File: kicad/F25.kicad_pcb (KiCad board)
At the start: 2 copper layers, 45 x 30 mm, 37 parts, among them J3 B2B-PH-K-S, J4 USB_C_Receptacle_USB2.0_16P, Q1 IRLML6244, SW1 RESET, SW2 BOOT, U1 MS5611-01BA, U2 MPU-6050, U4 ESP32-S3-WROOM-1-N8, U5 AP2112K-3.3

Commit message: MAJOR UPDATES
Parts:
- removed C11: 1uF, Capacitor_SMD:C_0402_1005Metric
- added C8: 10uF, Capacitor_SMD:C_0402_1005Metric, F.Cu at (177.4, 96.3)
- added Q2: DMG3415U, Package_TO_SOT_SMD:SOT-23, F.Cu at (173.1, 92.9)
- added R8: 100k, Capacitor_SMD:C_0402_1005Metric, F.Cu at (168.2, 107.4)
- added R9: 100k, Capacitor_SMD:C_0402_1005Metric, F.Cu at (163.5, 90.6)
- C10: value 1uF -> 10uF
- R5: value 10k -> 100k
- moved R5 21.5 mm to (177.4, 94.4), turned to 90 degrees
- moved C10 11.1 mm to (171.1, 98.7)
- moved R4 10.1 mm to (169.7, 103.5), turned to 90 degrees
- moved U5 2.05 mm to (173.2, 96.4), turned to 180 degrees
- moved LS1 0.60 mm to (175.7, 103.0), turned to -90 degrees
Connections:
- C1 pad 1: BAT- -> GND
- C10 pad 1: BAT+ -> GND
- C10 pad 2: BAT- -> +3V3
- C2 pad 1: BAT- -> GND
- C3 pad 2: BAT- -> GND
- C4 pad 1: BAT- -> GND
- C5 pad 1: BAT- -> GND
- C6 pad 2: BAT- -> GND
- C7 pad 2: BAT- -> GND
- C9 pad 2: BAT- -> GND
- CR1 pad 1: Net-(U5-VIN) -> Net-(Q2-S)
- CR1 pad 2: BAT+ -> /VBUS
- D1 pad 1: BAT- -> GND
- D2 pad 1: BAT- -> GND
- H1 pad 1: (no net) -> GND
- H2 pad 1: (no net) -> GND
- H3 pad 1: (no net) -> GND
- J3 pad 2: BAT- -> GND
- J4 pad A1: BAT- -> GND
- J4 pad A12: BAT- -> GND
- J4 pad A4: unconnected-(J4-VBUS-PadA4)_2 -> /VBUS
- J4 pad A9: unconnected-(J4-VBUS-PadA4)_1 -> /VBUS
- J4 pad B1: BAT- -> GND
- J4 pad B12: BAT- -> GND
- J4 pad B4: unconnected-(J4-VBUS-PadA4)_3 -> /VBUS
- J4 pad B9: unconnected-(J4-VBUS-PadA4) -> /VBUS
- J4 pad S1: BAT- -> GND
- Q1 pad 2: BAT- -> GND
- R12 pad 2: BAT- -> GND
- R5 pad 1: Net-(U4-GPIO3) -> Net-(Q2-S)
- R5 pad 2: +3V3 -> Net-(U5-EN)
- R6 pad 1: BAT- -> GND
- SW1 pad 1: BAT- -> GND
- SW2 pad 1: BAT- -> GND
- U1 pad 2: BAT- -> GND
- U1 pad 3: BAT- -> GND
- U2 pad 1: BAT- -> GND
- U2 pad 11: BAT- -> GND
- U2 pad 18: BAT- -> GND
- U2 pad 9: BAT- -> GND
- U4 pad 1: BAT- -> GND
- U4 pad 15: Net-(U4-GPIO3) -> unconnected-(U4-GPIO3-Pad15)
- U4 pad 40: BAT- -> GND
- U4 pad 41: BAT- -> GND
- U5 pad 1: Net-(U5-VIN) -> Net-(Q2-S)
- U5 pad 2: BAT- -> GND
- U5 pad 3: +3V3 -> Net-(U5-EN)
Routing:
- net /VBUS: track 0.00 -> 56.0 mm, vias 0 -> 4
- net GND: track 0.00 -> 39.3 mm, vias 0 -> 23
- net BAT-: track 35.9 -> 0.00 mm, vias 23 -> 0
- net Net-(Q2-S): track 0.00 -> 12.3 mm
- net /BUZZER: track 34.8 -> 39.1 mm
- net Net-(U5-EN): track 0.00 -> 3.47 mm
- net Net-(U5-VIN): track 3.44 -> 0.00 mm
- net /ESP_IO0: track 42.4 -> 45.6 mm
- net Net-(U4-GPIO3): track 2.04 -> 0.00 mm
- net Net-(Q1-D): track 6.25 -> 5.10 mm
- net Net-(LS1-Pad1): track 5.92 -> 7.04 mm
- added copper zone on B.Cu, net GND
- removed copper zone on B.Cu, net BAT-

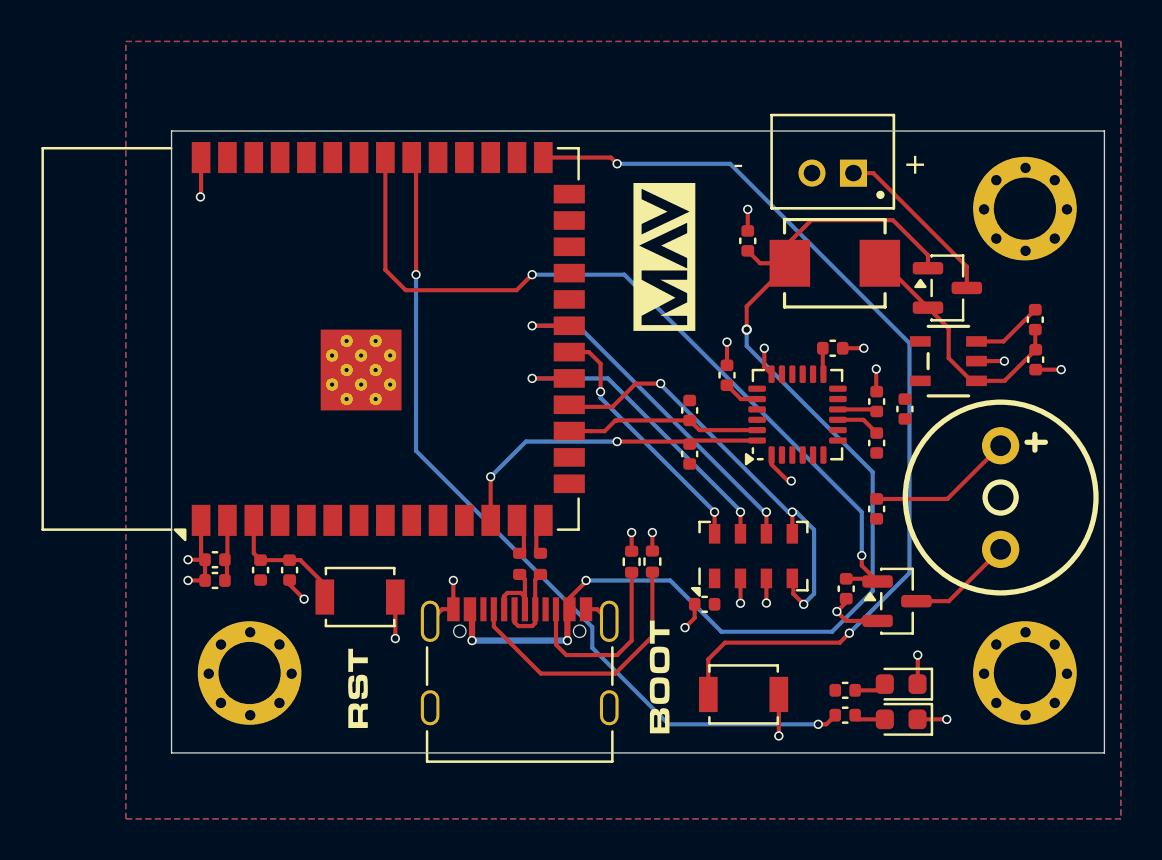
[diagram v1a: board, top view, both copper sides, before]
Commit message: MAJOR FIXES
Fixed Power circuitry
Added usb power support
Added pulldown to buzzer (thx taz)
Removed 10k pullup on gpio3
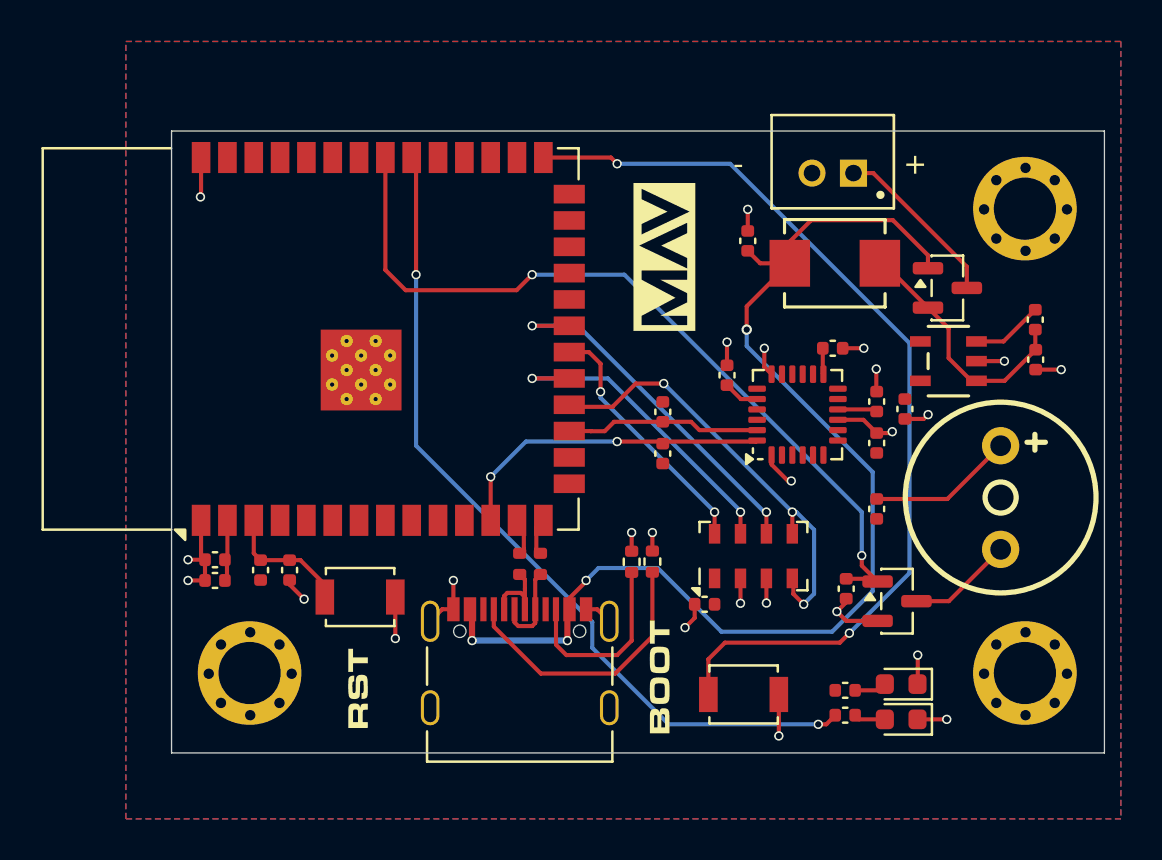
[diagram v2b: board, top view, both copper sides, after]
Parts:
- moved R2 1.30 mm to (159.4, 100.9)
- moved R3 1.30 mm to (159.4, 98.9)
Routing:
- net GND: track 39.3 -> 41.9 mm, vias 23 -> 25
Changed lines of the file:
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@@
 			)
 		)
+		(property "LCSC" "C7202986"
+			(at 0 0 0)
+			(unlocked yes)
+			(layer "F.Fab")
+			(hide yes)
+			(effects
+				(font
+					(size 1 1)
+					(thickness 0.15)
+				)
+			)
+		)
 		(property ki_fp_filters "SOT?23*")
 		(sheetname "/")
@@
 	(footprint "Capacitor_SMD:C_0402_1005Metric"
 		(layer "F.Cu")
-		(at 160.7 100.9 90)
+		(at 159.4 100.88 90)
 		(descr "Capacitor SMD 0402 (1005 Metric), square (rectangular) end terminal, IPC_7351 nominal, (Body size source: IPC-SM-782 page 76, https://www.pcb-3d.com/wordpress/wp-content/uploads/ipc-sm-782a_amendment_1_and_2.pdf), generated with kicad-footprint-generator")
 		(tags "capacitor")
@@
 	(footprint "Capacitor_SMD:C_0402_1005Metric"
 		(layer "F.Cu")
-		(at 160.7 98.8 -90)
+		(at 159.402235 98.866769 -90)
 		(descr "Capacitor SMD 0402 (1005 Metric), square (rectangular) end terminal, IPC_7351 nominal, (Body size source: IPC-SM-782 page 76, https://www.pcb-3d.com/wordpress/wp-content/uploads/ipc-sm-782a_amendment_1_and_2.pdf), generated with kicad-footprint-generator")
 		(tags "capacitor")
@@
 	)
 	(segment
-		(start 160.7 100.42)
-		(end 160.87 100.25)
+		(start 163.9 100.3)
+		(end 163.95 100.25)
 		(width 0.2)
 		(layer "F.Cu")
@@
 	(segment
 		(start 157.2 100.3)
-		(end 160.48 100.3)
-		(width 0.2)
-		(layer "F.Cu")
-		(net 7)
-	)
-	(segment
-		(start 160.48 100.3)
-		(end 160.7 100.52)
-		(width 0.2)
-		(layer "F.Cu")
-		(net 7)
-	)
-	(segment
-		(start 160.7 100.52)
-		(end 160.88 100.52)
-		(width 0.2)
-		(layer "F.Cu")
-		(net 7)
-	)
-	(segment
-		(start 160.87 100.25)
-		(end 163.95 100.25)
+		(end 163.9 100.3)
 		(width 0.2)
 		(layer "F.Cu")
@@
 	)
 	(segment
-		(start 161.17 99.75)
-		(end 163.95 99.75)
+		(start 157.053231 99.346769)
+		(end 160.766769 99.346769)
 		(width 0.2)
 		(layer "F.Cu")
@@
 	)
 	(segment
-		(start 157.2 99.28)
-		(end 160.7 99.28)
-		(width 0.2)
-		(layer "F.Cu")
-		(net 8)
-	)
-	(segment
-		(start 156.6 99.8)
-		(end 157.12 99.28)
+		(start 161.17 99.75)
+		(end 163.95 99.75)
 		(width 0.2)
 		(layer "F.Cu")
@@
 	)
 	(segment
-		(start 160.7 99.28)
+		(start 160.766769 99.346769)
 		(end 161.17 99.75)
 		(width 0.2)
@@
 	)
 	(segment
-		(start 155.92625 99.795)
-		(end 155.93125 99.8)
+		(start 156.6 99.8)
+		(end 157.053231 99.346769)
 		(width 0.2)
 		(layer "F.Cu")
@@
 	)
 	(segment
-		(start 157.12 99.28)
-		(end 157.2 99.28)
+		(start 155.92625 99.795)
+		(end 155.93125 99.8)
 		(width 0.2)
 		(layer "F.Cu")
@@
 	)
 	(segment
-		(start 159.76 107)
-		(end 162.234 109.474)
+		(start 167.569877 109.474)
+		(end 169.526 107.517877)
 		(width 0.2)
 		(layer "B.Cu")
@@
 	)
 	(segment
-		(start 162.234 109.474)
-		(end 167.569877 109.474)
+		(start 169.526 101.769877)
+		(end 163.45 95.693877)
 		(width 0.2)
 		(layer "B.Cu")
@@
 	)
 	(segment
-		(start 163.45 95.693877)
-		(end 163.45 94.9)
+		(start 155.7 107)
+		(end 156.3 106.4)
 		(width 0.2)
 		(layer "B.Cu")
@@
 	)
 	(segment
-		(start 155.7 107)
-		(end 159.76 107)
+		(start 163.45 95.693877)
+		(end 163.45 94.9)
 		(width 0.2)
 		(layer "B.Cu")
@@
 	)
 	(segment
-		(start 167.569877 109.474)
-		(end 169.526 107.517877)
+		(start 162.234 109.474)
+		(end 167.569877 109.474)
 		(width 0.2)
 		(layer "B.Cu")
@@
 	)
 	(segment
-		(start 169.526 101.769877)
-		(end 163.45 95.693877)
+		(start 156.3 106.4)
+		(end 159.16 106.4)
 		(width 0.2)
 		(layer "B.Cu")
@@
 	)
 	(segment
+		(start 159.16 106.4)
+		(end 162.234 109.474)
+		(width 0.2)
+		(layer "B.Cu")
+		(net 31)
+	)
+	(segment
 		(start 151.9 107.6)
 		(end 152.55 107.6)
@@
 	)
 	(segment
+		(start 171.99 99.21)
+		(end 171.08 99.21)
+		(width 0.2)
+		(layer "F.Cu")
+		(net 38)
+	)
+	(segment
 		(start 137.42 107)
 		(end 136.5 107)
@@
 	)
 	(segment
+		(start 169.719999 99.89)
+		(end 170.405108 99.89)
+		(width 0.2)
+		(layer "F.Cu")
+		(net 38)
+	)
+	(segment
 		(start 156.24 108.39)
 		(end 156.82 108.97)
@@
 	)
 	(segment
+		(start 172.2 99)
+		(end 171.99 99.21)
+		(width 0.2)
+		(layer "F.Cu")
+		(net 38)
+	)
+	(segment
 		(start 137.32 106)
 		(end 136.5 106)
@@
 	)
 	(segment
+		(start 170.405108 99.89)
+		(end 170.471007 99.824101)
+		(width 0.2)
+		(layer "F.Cu")
+		(net 38)
+	)
+	(segment
+		(start 171.08 99.21)
+		(end 171.08 99.215108)
+		(width 0.2)
+		(layer "F.Cu")
+		(net 38)
+	)
+	(segment
 		(start 163.15 106.9)
 		(end 163.15 108.1)
@@
 	)
 	(via
+		(at 170.471007 99.824101)
+		(size 0.45)
+		(drill 0.3)
+		(layers "F.Cu" "B.Cu")
+		(free yes)
+		(net 38)
+	)
+	(via
 		(at 149.3 107)
 		(size 0.45)
@@
 	)
 	(via
+		(at 172.2 99)
+		(size 0.45)
+		(drill 0.3)
+		(layers "F.Cu" "B.Cu")
+		(free yes)
+		(net 38)
+	)
+	(via
 		(at 165 114.5)
 		(size 0.45)
@@
 	)
 	(segment
+		(start 156.82 109.57)
+		(end 156.82 108.97)
+		(width 0.3)
+		(layer "B.Cu")
+		(net 38)
+	)
+	(segment
 		(start 154.25 110.1)
 		(end 154.75 110.6)
@@
 	)
 	(segment
-		(start 147.5 100.75)
-		(end 156 109.25)
+		(start 159.69 113.94)
+		(end 166.9 113.94)
 		(width 0.2)
 		(layer "B.Cu")
@@
 	)
 	(segment
-		(start 156 109.25)
+		(start 156 109)
 		(end 156 110.25)
 		(width 0.2)
@@
 	)
 	(segment
-		(start 156 110.25)
-		(end 159.69 113.94)
+		(start 147.5 100.5)
+		(end 156 109)
 		(width 0.2)
 		(layer "B.Cu")
@@
 	)
 	(segment
-		(start 159.69 113.94)
-		(end 166.9 113.94)
+		(start 156 110.25)
+		(end 159.69 113.94)
 		(width 0.2)
 		(layer "B.Cu")
@@
 	(segment
 		(start 147.5 92.25)
-		(end 147.5 100.75)
+		(end 147.5 100.5)
 		(width 0.2)
 		(layer "B.Cu")
@@
 	)
 	(segment
-		(start 154.991 98.626)
-		(end 154.89 98.525)
+		(start 156.974 98.626)
+		(end 154.991 98.626)
 		(width 0.2)
 		(layer "F.Cu")
@@
 	)
 	(segment
-		(start 166.2 108.15)
-		(end 165.7 107.65)
+		(start 154.991 98.626)
+		(end 154.89 98.525)
 		(width 0.2)
 		(layer "F.Cu")
@@
 	)
 	(segment
-		(start 159.3 97.5)
-		(end 158.1 97.5)
+		(start 166.2 108.15)
+		(end 165.7 107.65)
 		(width 0.2)
 		(layer "F.Cu")
@@
 	)
 	(segment
-		(start 165.65 103.7)
-		(end 165.65 104.75)
+		(start 158.1 97.5)
+		(end 156.974 98.626)
 		(width 0.2)
 		(layer "F.Cu")
@@
 	)
 	(segment
-		(start 158.1 97.5)
-		(end 156.974 98.626)
+		(start 159.449042 97.5)
+		(end 158.1 97.5)
 		(width 0.2)
 		(layer "F.Cu")
@@
 	)
 	(segment
-		(start 156.974 98.626)
-		(end 154.991 98.626)
+		(start 165.65 103.7)
+		(end 165.65 104.75)
 		(width 0.2)
 		(layer "F.Cu")
@@
 	)
 	(via
-		(at 159.3 97.5)
+		(at 159.449042 97.5)
 		(size 0.45)
 		(drill 0.3)
@@
 	)
 	(segment
-		(start 166.7 107.645836)
-		(end 166.7 104.556123)
+		(start 165.65 103.7)
+		(end 165.843877 103.7)
 		(width 0.2)
 		(layer "B.Cu")
@@
 	)
 	(segment
-		(start 159.3 97.55)
-		(end 159.3 97.5)
+		(start 166.7 104.556123)
+		(end 166.7 107.645836)
 		(width 0.2)
 		(layer "B.Cu")
@@
 	)
 	(segment
-		(start 166.186345 108.159491)
-		(end 166.7 107.645836)
+		(start 165.843877 103.7)
+		(end 166.7 104.556123)
 		(width 0.2)
 		(layer "B.Cu")
@@
 	)
 	(segment
-		(start 165.843877 103.7)
-		(end 165.45 103.7)
+		(start 159.449042 97.5)
+		(end 159.599042 97.65)
 		(width 0.2)
 		(layer "B.Cu")
@@
 	)
 	(segment
-		(start 165.45 103.7)
-		(end 159.3 97.55)
+		(start 159.599042 97.65)
+		(end 159.6 97.65)
 		(width 0.2)
 		(layer "B.Cu")
@@
 	)
 	(segment
-		(start 166.7 104.556123)
-		(end 165.843877 103.7)
+		(start 166.7 107.645836)
+		(end 166.186345 108.159491)
+		(width 0.2)
+		(layer "B.Cu")
+		(net 57)
+	)
+	(segment
+		(start 159.6 97.65)
+		(end 165.65 103.7)
 		(width 0.2)
 		(layer "B.Cu")
